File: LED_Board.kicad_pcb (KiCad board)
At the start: 2 copper layers, 95 x 45 mm, 16 parts, among them SW101 SW_PUSH

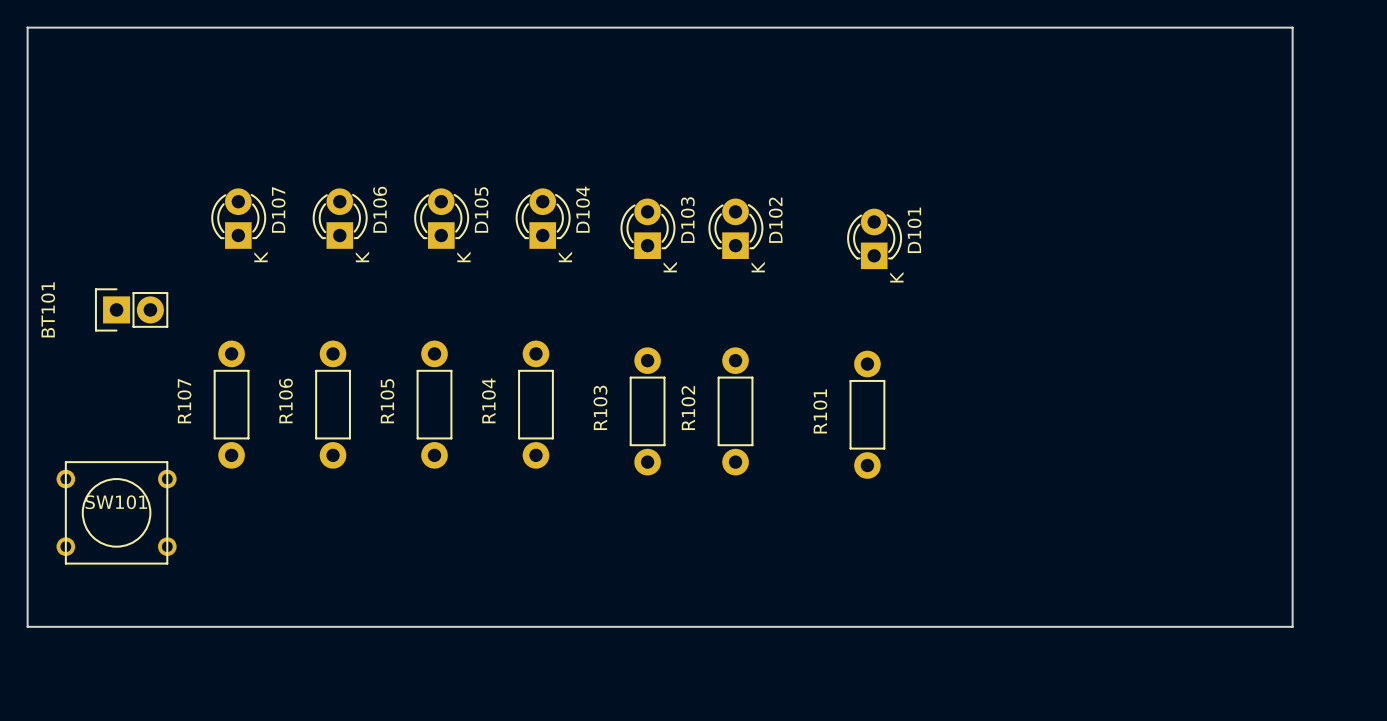
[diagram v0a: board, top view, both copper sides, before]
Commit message: add logo
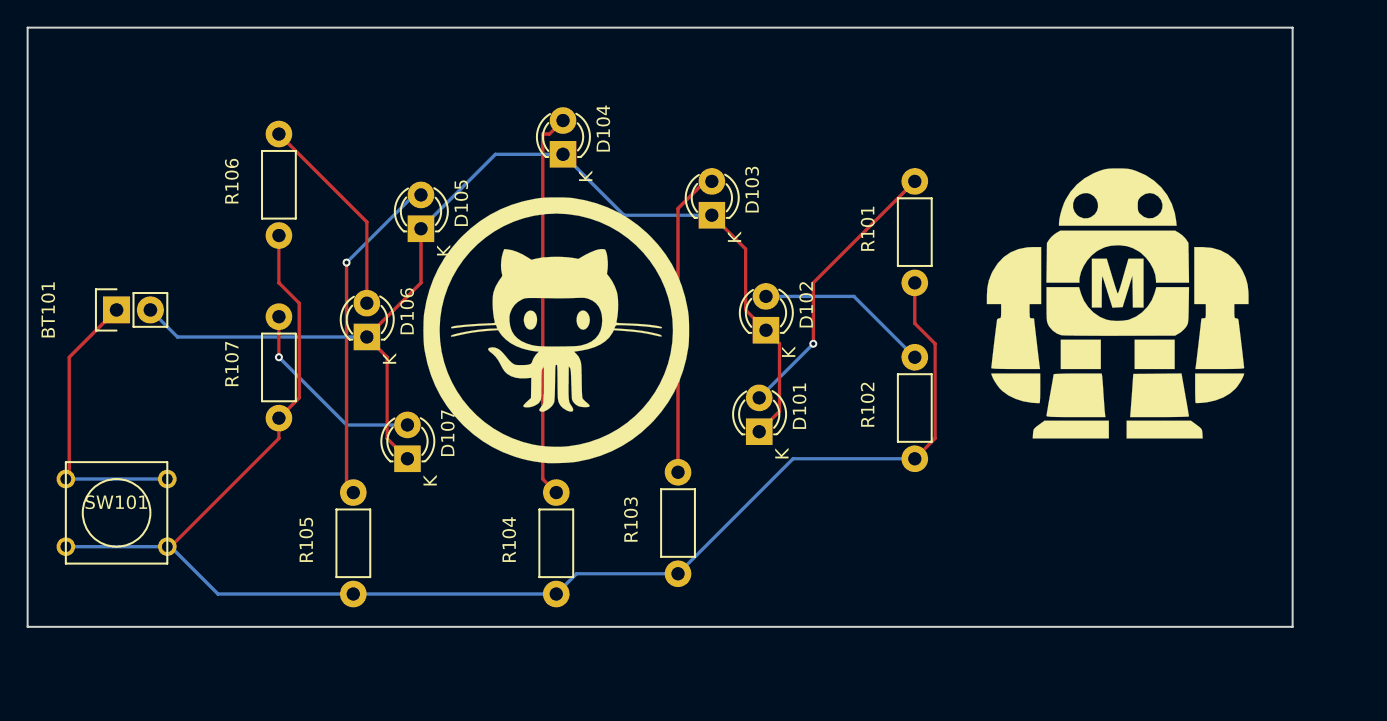
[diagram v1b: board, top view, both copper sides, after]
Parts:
- added G***: LOGO, logo:GitHub_20mm, F.Cu at (139.7, 77.7)
- added G***: LOGO, logo:maker_bot, F.Cu at (181.9, 75.7)
- moved D107 21.0 mm to (128.5, 87.4)
- moved R106 17.0 mm to (118.9, 70.6)
- moved D101 15.8 mm to (154.9, 85.3)
- moved R101 14.2 mm to (166.6, 74.2)
- moved R102 13.5 mm to (166.6, 87.4)
- moved R105 12.1 mm to (124.5, 97.5)
- moved R104 10.5 mm to (139.7, 97.5)
- moved R103 8.69 mm to (148.8, 96.0)
- moved D106 7.89 mm to (125.5, 78.2)
- moved D102 6.75 mm to (155.4, 77.7)
- moved D104 6.28 mm to (140.2, 64.5)
- moved D103 5.34 mm to (151.4, 69.1)
- moved R107 4.52 mm to (118.9, 84.3)
- moved D105 1.61 mm to (129.5, 70.1)
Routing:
- net +BATT: track 0.00 -> 112.2 mm
- net GND: track 0.00 -> 82.4 mm
- net Net-(D104-Pad2): track 0.00 -> 29.3 mm
- net Net-(D105-Pad2): track 0.00 -> 25.2 mm, vias 0 -> 1
- net Net-(D103-Pad2): track 0.00 -> 23.2 mm
- net Net-(BT101-Pad1): track 0.00 -> 22.0 mm
- net Net-(D101-Pad2): track 0.00 -> 21.1 mm, vias 0 -> 1
- net Net-(D106-Pad2): track 0.00 -> 15.4 mm
- net Net-(D107-Pad2): track 0.00 -> 14.8 mm, vias 0 -> 1
- net Net-(D102-Pad2): track 0.00 -> 13.1 mm

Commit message: PCB sizze 45*95 -> 50 * 100
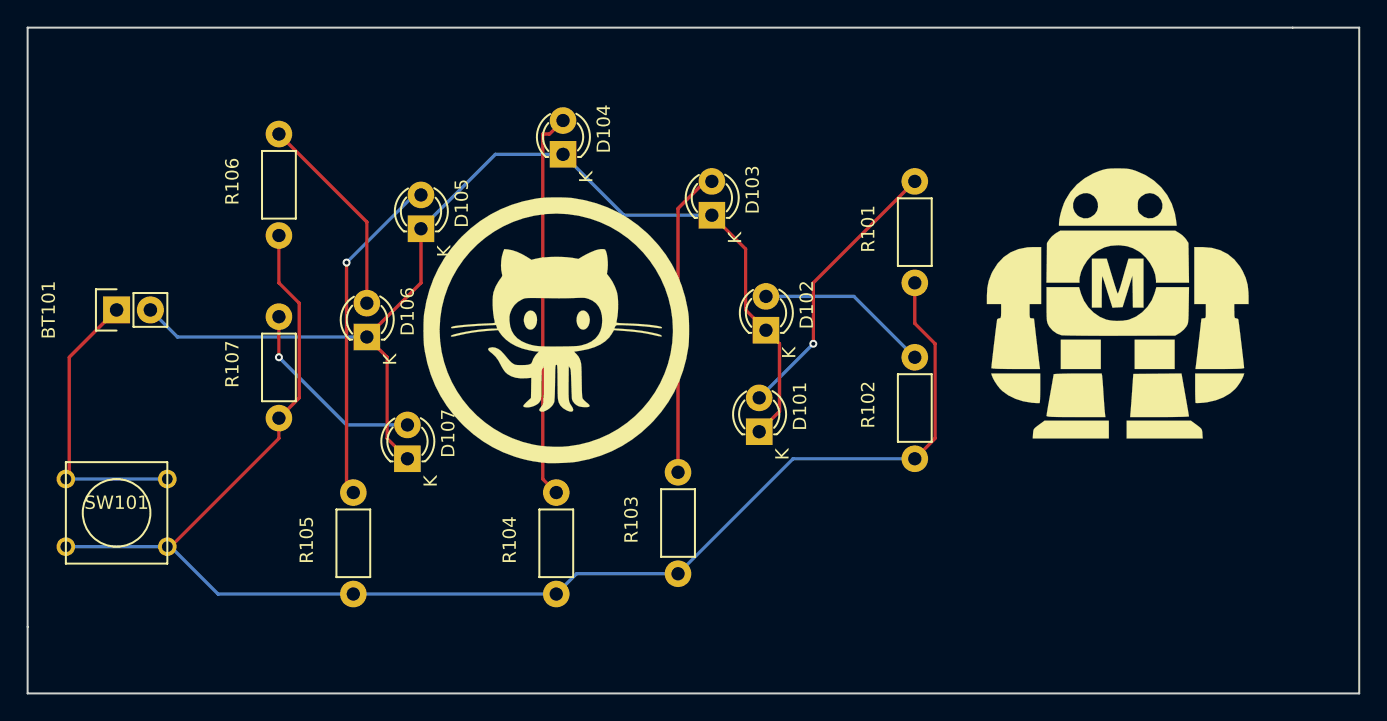
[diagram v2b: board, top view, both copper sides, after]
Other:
- board size 95 x 45 mm -> 100 x 50 mm
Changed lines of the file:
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@@
-(kicad_pcb (version 4) (host pcbnew 4.0.1-stable)
+(kicad_pcb (version 4) (host pcbnew 4.0.2-stable)
   (general
     (links 24)
     (no_connects 0)
-    (area 99.924999 54.924999 195.075001 100.075001)
+    (area 99.924999 54.924999 200.075001 105.075001)
     (thickness 1.6)
-    (drawings 4)
+    (drawings 6)
     (tracks 65)
     (zones 0)
@@
       (xy -0.136593 -10.118975) (xy 0 -10.119091) (xy 0.374636 -10.115306)) (layer F.SilkS) (width 0.01))
   )
+  (gr_line (start 100 105) (end 100 100) (angle 90) (layer Edge.Cuts) (width 0.15))
+  (gr_line (start 200 105) (end 100 105) (angle 90) (layer Edge.Cuts) (width 0.15))
+  (gr_line (start 200 55) (end 200 105) (angle 90) (layer Edge.Cuts) (width 0.15))
+  (gr_line (start 195 55) (end 200 55) (angle 90) (layer Edge.Cuts) (width 0.15))
   (gr_line (start 100 100) (end 100 55) (angle 90) (layer Edge.Cuts) (width 0.15))
-  (gr_line (start 195 100) (end 100 100) (angle 90) (layer Edge.Cuts) (width 0.15))
-  (gr_line (start 195 55) (end 195 100) (angle 90) (layer Edge.Cuts) (width 0.15))
   (gr_line (start 195 55) (end 100 55) (angle 90) (layer Edge.Cuts) (width 0.15))
   (segment (start 129.54 70.104) (end 135.128 64.516) (width 0.25) (layer B.Cu) (net 1) (status 80000))
